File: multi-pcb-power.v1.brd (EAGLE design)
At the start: 72.1 x 32.7 mm, 24 parts, among them Q5 TIP136, T2 BC618, X1 2.52B-ZR, X2 2.52B-ZR, X3 2.52B-ZR, X4 2.54B-ZR

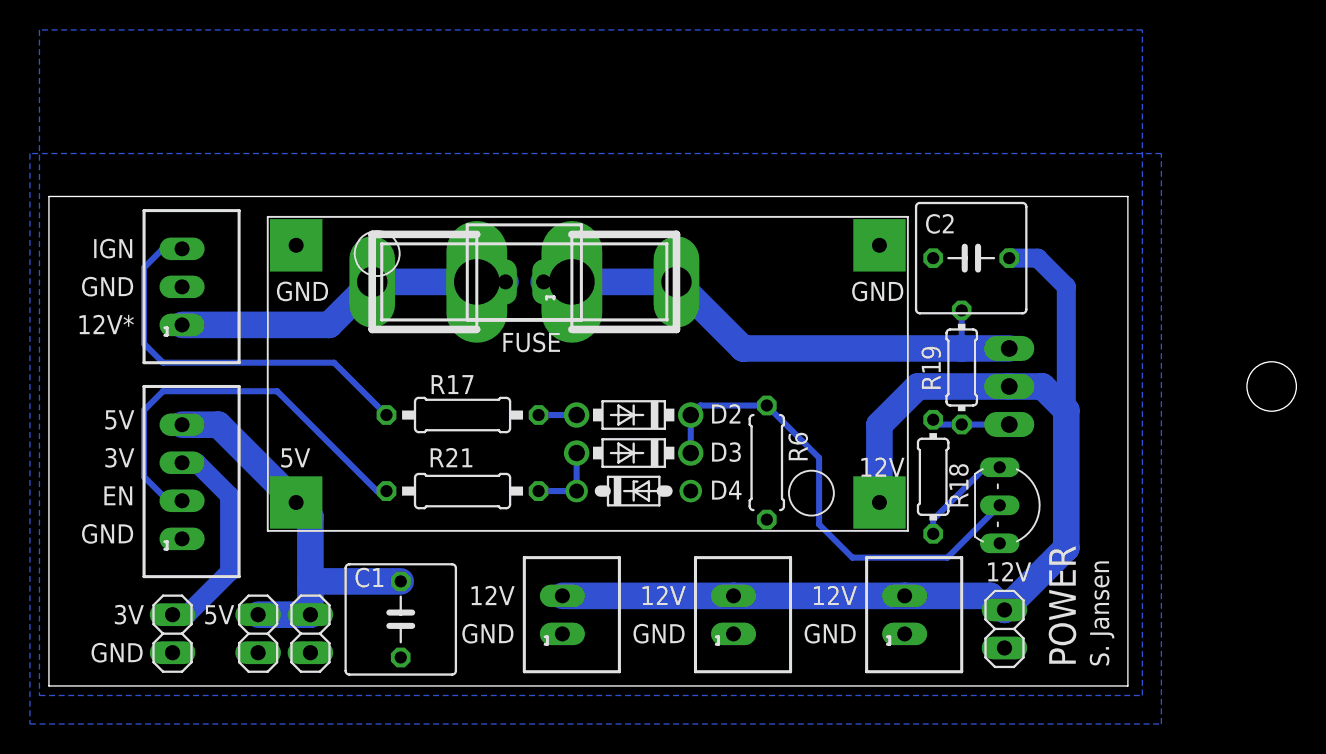
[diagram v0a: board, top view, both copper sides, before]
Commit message: Fixed PSU and fuse footprints. Also updated layout and added buffer capacitors.
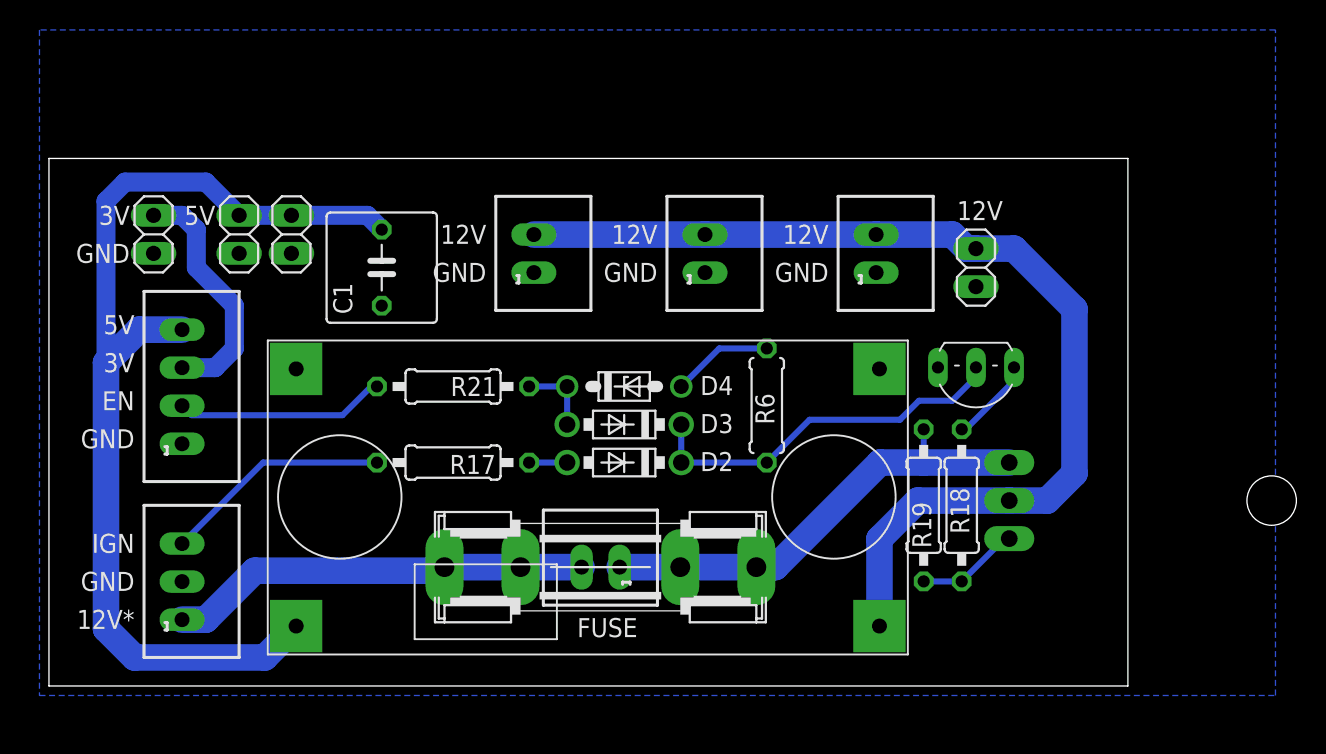
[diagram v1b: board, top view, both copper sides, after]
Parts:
- removed C2: (no value), rcl:C050-075X075
- removed U$1: FUSE, samuel:FB-5X20
- added F1: 2A, fuse:SHK20L
- R18, R19: device rcl:0204/7 -> rcl:0207/10
- moved JP_PWR_3V3 26.7 mm to (6.99, 30.2)
- moved JP_PWR_5V_1 26.7 mm to (16.2, 30.2)
- moved JP_PWR_5V_2 26.7 mm to (12.7, 30.2)
- moved JP_PWR_12V 24.2 mm to (61.9, 27.9)
- moved X1 24.2 mm to (55.2, 28.9)
- moved X2 24.2 mm to (32.4, 28.9)
- moved X3 24.2 mm to (43.8, 28.9)
- moved C1 23.5 mm to (22.2, 27.9)
- moved FUSE 19.7 mm to (36.8, 7.94)
- moved PWR 19.7 mm to (8.89, 6.99)
- moved R19 9.55 mm to (58.4, 12.1)
- moved T2 8.44 mm to (61.9, 20.0), turned to 180 degrees
- moved U$4 8.26 mm to (35.8, 13.0)
- moved Q5 7.62 mm to (70.5, 12.4)
- moved D4 7.01 mm to (38.4, 20.0)
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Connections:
- net +12V: now also F1.2A; no longer U$1.P$3, U$1.P$4
- net GND: no longer C2.2
- net N$21: now also F1.1A; no longer U$1.P$1, U$1.P$2
- net PWR_IN+: no longer C2.1
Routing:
- net +5V: track 27.2 -> 69.2 mm
- net PWR_ENABLE: track 27.1 -> 14.1 mm
- net IGNITION: track 26.3 -> 15.3 mm
- net PWR_IN+: track 77.2 -> 69.8 mm
- net GND: track 0.00 -> 6.77 mm
- net N$5: track 31.7 -> 25.2 mm
- net +12V: track 22.8 -> 28.1 mm
- net N$21: track 35.5 -> 31.1 mm
- net +3V3: track 14.2 -> 16.3 mm
- net N$14: track 5.21 -> 6.90 mm
- net N$15: track 6.84 -> 5.73 mm
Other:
- board size 72.1 x 32.7 mm -> 72.1 x 35.2 mm
- board text removed: "POWER"
- board text removed: "S. Jansen"
